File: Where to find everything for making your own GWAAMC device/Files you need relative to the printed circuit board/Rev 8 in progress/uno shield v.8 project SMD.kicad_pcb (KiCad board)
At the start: 2 copper layers, 68.6 x 53.3 mm, 107 parts, among them J1 Conn_3.5mm, J2 Power, J3 Analog, J4 Digital, J5 Digital, J6 Conn_01x09_Female, J6_A7,A6 Conn_01x02_gender_unknown, J7_A7,A6 Conn_01x02_Female, J9 TE_1-2328702-0, P1 CONN_01X01, P2 CONN_01X01, P3 CONN_01X01, P4 CONN_01X01, Q1 MMBF5460 (2N5460), Q2 MMBF5460 (2N5460), Q3 DMN601K-7, Q4 DMN601K-7, Q5 DMN601K-7, Q6 DMN601K-7, Q7 DMN601K-7, U1 3V LDO, U10 MCP4262-502E/UN, U11 MCP4262-502E/UN, U12 MCP4262-502E/UN, U13 MCP4262-502E/UN, U14 MCP4262-502E/UN, U15 MCP4262-502E/UN, U16 MCP4262-502E/UN, U17 MCP4262-502E/UN, U18 MCP4262-502E/UN, U19 MCP4262-502E/UN, U2 AD8244ARMZ, U20 MCP4262-502E/UN, U21 MCP4262-502E/UN, U22 MCP4262-502E/UN, U23 MCP4262-502E/UN, U24 MCP4262-502E/UN, U25 MCP4262-502E/UN, U26 MCP4262-502E/UN, U27 MCP4262-502E/UN, U28 MCP4262-502E/UN, U29 MCP4262-502E/UN, U3 ADL5315ACPZ-R7, U30 MCP4262-502E/UN, U31 MCP4262-502E/UN, U32 MCP4262-502E/UN, U33 MCP4262-502E/UN, U4 REF200AU, U5 LM334M, U6 LM334M, U7 MCP4262-503E/UN, U8 - U32 all in parallel MCP4262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, U9 MCP4262-502E/UN

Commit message: In the latest state of progress...
...definitely not in working state, but where I'll resume work when I get back to things.
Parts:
- moved U8 0.52 mm to (162.4, 104.7)
- moved U7 0.46 mm to (163.0, 104.9)
- moved J9 0.08 mm to (167.9, 106.8)
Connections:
- J9 pad 10: /7 -> /8
- J9 pad 2: /U8-Pad5 -> /U8-Pad7
- J9 pad 3: /U8-Pad7 -> /U8-Pad8
- J9 pad 4: /U8-Pad8 -> /U8-Pad5
- J9 pad 8: /SCK(1) -> /MOSI(1)
- J9 pad 9: /MOSI(1) -> /SCK(1)
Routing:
- net /6(**): track 41.8 -> 92.5 mm, vias 3 -> 10
- net /8: track 57.6 -> 10.6 mm, vias 8 -> 1
- net +5V: track 291.7 -> 248.8 mm, vias 31 -> 29
- net /U8-Pad6: track 47.9 -> 38.6 mm
- net /U8-Pad8: track 12.1 -> 18.8 mm
- net GNDD: track 208.7 -> 202.6 mm, vias 40 -> 42
- net /U8-Pad5: track 2.58 -> 8.50 mm, vias 0 -> 1
- net /U8-Pad7: track 8.71 -> 14.3 mm
- net Net-(Q2-Pad2): track 45.4 -> 40.7 mm
- net /MOSI(1): track 19.1 -> 21.7 mm
- net /7: track 53.5 -> 51.3 mm, vias 4 -> 2
- net Net-(U5-Pad1): track 5.61 -> 3.69 mm
- net /1st_stage_guard_trace: track 357.1 -> 355.3 mm, vias 18 -> 19

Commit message: In the latest state of progress...
...definitely not in working state, but where I'll resume work when I get back to things.
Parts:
- moved R17 0.21 mm to (157.6, 102.7)
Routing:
- net /8: track 10.6 -> 52.7 mm, vias 1 -> 5
- net /6(**): track 92.5 -> 62.0 mm, vias 10 -> 8
- net /1st_stage_guard_trace: track 355.3 -> 365.3 mm, vias 19 -> 18
- net /U8-Pad6: track 38.6 -> 32.3 mm, vias 6 -> 4
- net GNDD: track 202.6 -> 208.8 mm
- net Net-(U5-Pad1): track 3.69 -> 8.89 mm, vias 1 -> 2
- net /U8-Pad7: track 14.3 -> 19.1 mm, vias 1 -> 2
- net Net-(Q2-Pad2): track 40.7 -> 44.8 mm
- net +5V: track 248.8 -> 252.4 mm
- net /7: track 51.3 -> 49.3 mm
- net GNDA: track 199.5 -> 198.2 mm
- net /Rx: track 56.3 -> 55.0 mm
- net /U8-Pad8: track 18.8 -> 18.2 mm

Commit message: In the latest state of progress...
I HAVEN'T DESIGNED THE FLEX CIRCUIT BOARD FOR U9-U33, THE PARALLELED MCP4262-502 DPOTS, BUT THE REST OF THESE FILES ARE COMPLETED AND FUNCTIONAL TO THE BEST OF MY UNDERSTANDING, INCLUDING THE MAIN BOARD BEING COMPLETE AND WORKING.
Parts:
- removed U10, U11, U12, U13, U14, U15, U16, U17, U18, U19, U20, U21, U22, U23, U24, U25, U26, U27, U28, U29, U30, U31, U32, U33, U9: MCP4262-502E/UN, Package_SO:MSOP-10_3x3mm_P0.5mm
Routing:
- net /8: track 52.7 -> 44.3 mm, vias 5 -> 4
- net +5V: track 252.4 -> 246.3 mm, vias 29 -> 28
- net /U8-Pad8: track 18.2 -> 12.6 mm, vias 2 -> 1
- net /SCK(1): track 21.2 -> 16.1 mm, vias 2 -> 1
- net /U8-Pad7: track 19.1 -> 14.3 mm, vias 2 -> 1
- net GNDD: track 208.8 -> 204.4 mm, vias 42 -> 41
- net /MOSI(1): track 22.2 -> 17.8 mm, vias 2 -> 1
- net /U8-Pad6: track 32.3 -> 28.0 mm, vias 4 -> 3
- net /7: track 49.3 -> 46.7 mm
- net /1st_stage_guard_trace: track 365.3 -> 367.7 mm
- net (no net): vias 1 -> 0
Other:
- board text added: "All place-assist holes are for use w/straight pins; you could delay sealing them until their parts get placed"
- board text added: "NOTICE: These 10 contacts must V V remain untinned!"
- board text added: "Place-assist holes given may be needed esp. on HASL finishes"
- board text added: "R17"
- board text added: "R18"
- board text added: "Solder to U3 through hole^"
- board text removed: "All place-assist holes are for use w/straight pins; you could delay sealing them un- til their parts get placed"
- board text removed: "Place-assist holes are esp. for HASL"
- board text removed: "Solder to U2 through hole^"

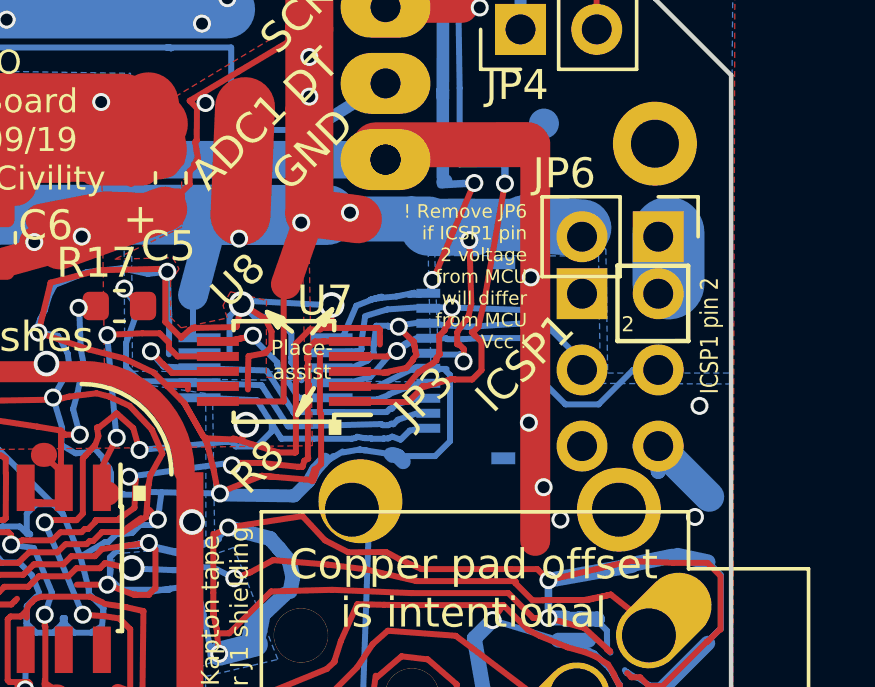
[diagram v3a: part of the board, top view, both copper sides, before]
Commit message: Untested while awaiting bare PCB boards....
These KiCad and zipped gerber files are fully designed but not yet tested while I await the bare boards on order now.  I'm estimating mid- to late-October will see the final evaluation of operation of the entire device.  Shortly after that, I would expect to demonstrate its concepts and operation via YouTube and personal travel.
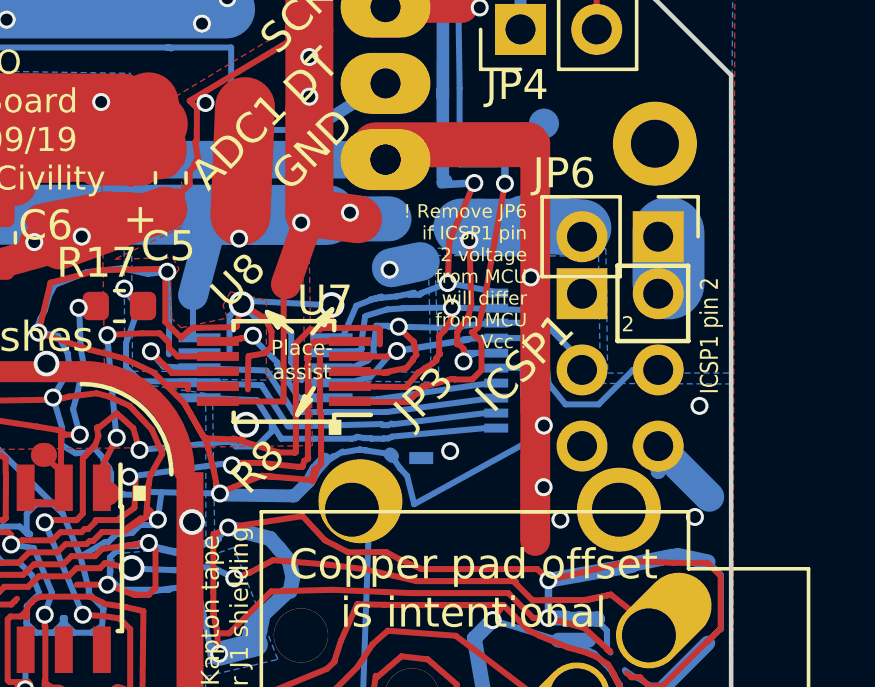
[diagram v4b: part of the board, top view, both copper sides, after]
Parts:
- moved J9 5.04 mm to (170.1, 102.3), turned to 90 degrees
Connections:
- ICSP1 pad 1: (no net) -> Net-(ICSP1-Pad1)
- ICSP1 pad 5: (no net) -> Net-(ICSP1-Pad5)
- J1 pad R: (no net) -> Net-(J1-PadR)
- J1 pad TN: (no net) -> Net-(J1-PadTN)
- J2 pad 2: (no net) -> Net-(J2-Pad2)
- J2 pad 3: (no net) -> Net-(J2-Pad3)
- J2 pad 4: (no net) -> Net-(J2-Pad4)
- J2 pad 8: (no net) -> Net-(J2-Pad8)
- J3 pad 5: (no net) -> Net-(J3-Pad5)
- J3 pad 6: (no net) -> Net-(J3-Pad6)
- J4 pad 1: (no net) -> Net-(J4-Pad1)
- J4 pad 2: (no net) -> Net-(J4-Pad2)
- J4 pad 3: (no net) -> Net-(J4-Pad3)
- J4 pad 5: (no net) -> Net-(J4-Pad5)
- J4 pad 6: (no net) -> Net-(J4-Pad6)
- J4 pad 7: (no net) -> Net-(J4-Pad7)
- J4 pad 8: (no net) -> Net-(J4-Pad8)
- J4 pad 9: (no net) -> Net-(J4-Pad9)
- J5 pad 4: (no net) -> Net-(J5-Pad4)
- J6 pad 9: (no net) -> Net-(J6-Pad9)
- J9 pad 1: /U8-Pad6 -> /8
- J9 pad 10: /8 -> /U8-Pad6
- J9 pad 2: /U8-Pad7 -> /SCK(1)
- J9 pad 3: /U8-Pad8 -> /MOSI(1)
- J9 pad 4: /U8-Pad5 -> GNDD
- J9 pad 5: /1st_stage_guard_trace -> +5V
- J9 pad 6: +5V -> /1st_stage_guard_trace
- J9 pad 7: GNDD -> /U8-Pad5
- J9 pad 8: /MOSI(1) -> /U8-Pad8
- J9 pad 9: /SCK(1) -> /U8-Pad7
- JP10 pad 3: (no net) -> Net-(JP10-Pad3)
- JP11 pad 3: (no net) -> Net-(JP11-Pad3)
- JP8 pad 3: (no net) -> Net-(JP8-Pad3)
- JP9 pad 3: (no net) -> Net-(JP9-Pad3)
- P1 pad 1: (no net) -> Net-(P1-Pad1)
- P2 pad 1: (no net) -> Net-(P2-Pad1)
- P3 pad 1: (no net) -> Net-(P3-Pad1)
- P4 pad 1: (no net) -> Net-(P4-Pad1)
- U3 pad 3: (no net) -> Net-(U3-Pad3)
- U4 pad 6: (no net) -> Net-(U4-Pad6)
- U7 pad 9: (no net) -> Net-(U7-Pad9)
- U8 pad 9: (no net) -> Net-(U8-Pad9)
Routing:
- net /U8-Pad6: track 28.0 -> 30.2 mm
- net /U8-Pad5: track 8.74 -> 10.9 mm
- net /U8-Pad7: track 14.3 -> 16.5 mm
- net /1st_stage_guard_trace: track 367.7 -> 369.9 mm
- net /8: track 44.3 -> 46.4 mm
- net /U8-Pad8: track 12.6 -> 14.4 mm
- net GNDD: track 204.4 -> 205.5 mm, vias 41 -> 43
- net +5V: track 246.3 -> 245.5 mm

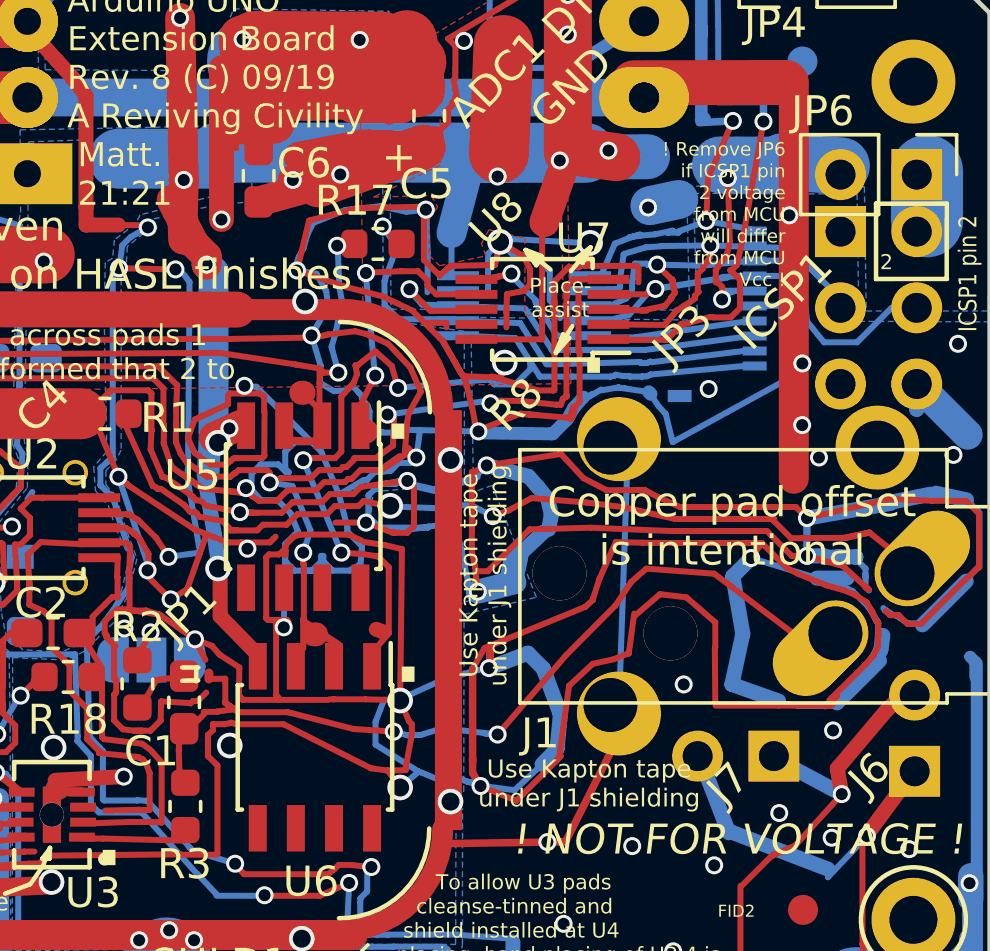
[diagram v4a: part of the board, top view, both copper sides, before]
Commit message: Untested while awaiting bare PCB boards...
These KiCad and zipped gerber files are fully designed but not yet tested while I await the bare boards on order now.  I'm estimating mid- to late-October will see the final evaluation of operation of the entire device.  Shortly after that, I would expect to demonstrate its concepts and operation via YouTube and personal travel.
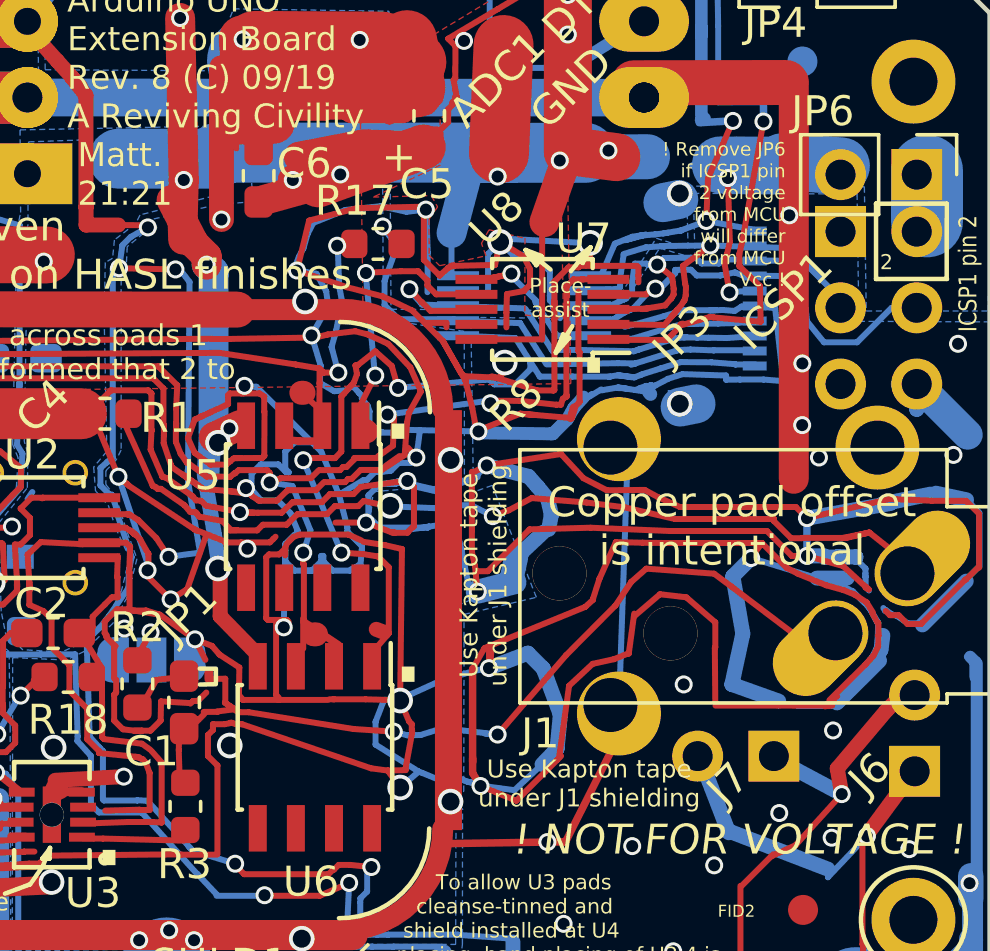
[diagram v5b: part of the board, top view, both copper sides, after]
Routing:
- net /1st_stage_guard_trace: track 369.9 -> 373.4 mm
- net /U8-Pad5: track 10.9 -> 12.0 mm
- net +5V: track 245.5 -> 244.4 mm
- net /7: track 46.7 -> 47.6 mm
- net GNDD: track 205.5 -> 206.3 mm
- net /U8-Pad6: track 30.2 -> 30.8 mm
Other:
- board text added: "NOTICE: These 2 support contacts must get soldered through and through to other <-- board side-->"
- board text removed: "NOTICE: These 10 contacts must V V remain untinned!"
